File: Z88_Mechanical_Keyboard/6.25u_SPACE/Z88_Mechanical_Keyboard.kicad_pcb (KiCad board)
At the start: 2 copper layers, 289 x 110 mm, 68 parts, among them SW1 SHIFT_RH, SW10 SHIFT_LH, SW11 SPACE, SW12 LEFT, SW13 RIGHT, SW14 DOWN, SW15 UP, SW16 ENTER, SW17 ESC, SW18 TAB, SW19 ONE, SW2 HELP, SW20 2, SW21 3, SW22 4, SW23 5, SW24 6, SW25 INDEX, SW26 DIAMOND, SW27 Q, SW28 W, SW29 E, SW3 [, SW30 R, SW31 T, SW32 Y, SW33 CAPS_LOCK, SW34 MENU, SW35 A, SW36 S, SW37 D, SW38 F, SW39 G, SW4 ], SW40 H, SW41 DOT, SW42 COMMA, SW43 Z, SW44 X, SW45 C, SW46 V, SW47 B, SW48 N, SW49 /FORWSLASH/, SW5 UNDERSCORE, SW50 SEMICOLON, SW51 L, SW52 M, SW53 K, SW54 J, SW55 U, SW56 7, SW57 GBP, SW58 DOUBLE_QUOTE, SW59 ZERO, SW6 EQUALS, SW60 P, SW61 9, SW62 O, SW63 I, SW64 8, SW7 \BACKSLASH\, SW8 DELETE, SW9 SQUARE

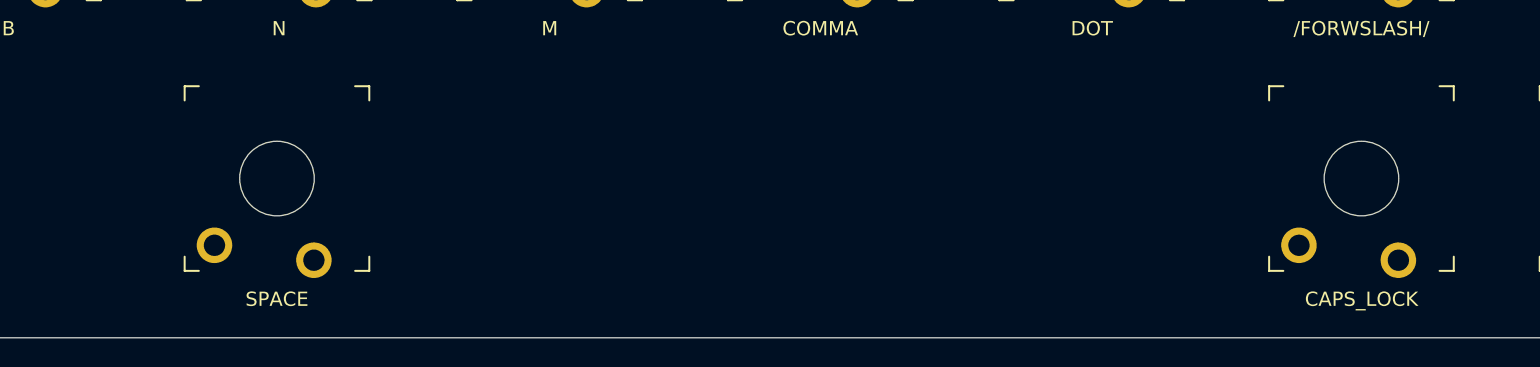
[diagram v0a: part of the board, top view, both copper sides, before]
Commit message: 6.25u & 7u SPACE bar lengths
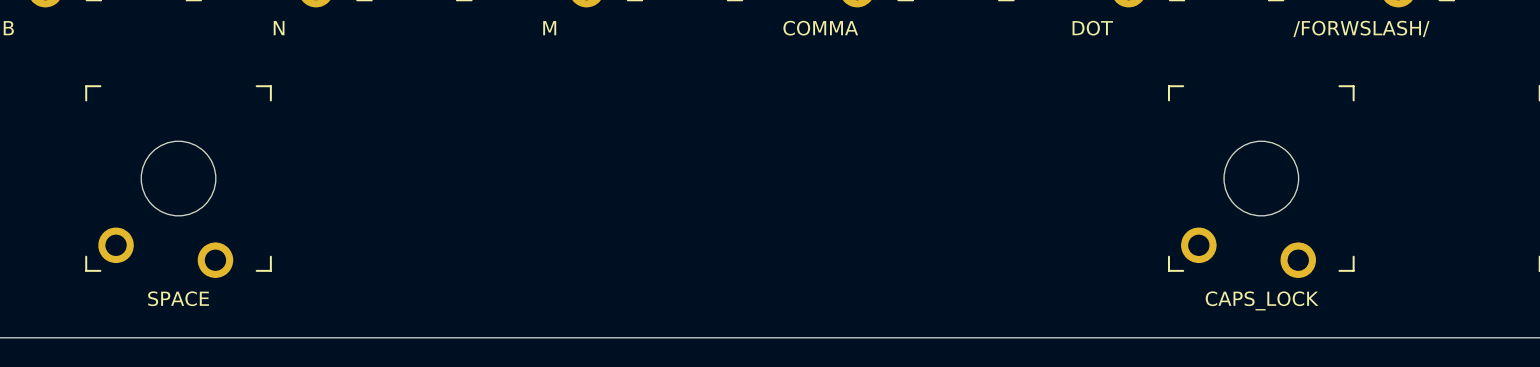
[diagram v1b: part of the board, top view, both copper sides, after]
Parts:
- moved SW33 7.05 mm to (276.9, 187.7)
- moved SW11 6.93 mm to (200.7, 187.7)
